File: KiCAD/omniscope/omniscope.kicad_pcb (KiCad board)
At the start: 2 copper layers, 132.8 x 90.8 mm, 40 parts, among them J1 Conn_01x08_Male, J2 Conn_01x02_Male, J3 Conn_01x02_Male, J4 Conn_01x08_Male, J5 Conn_01x08_Male, J6 Conn_01x08_Male, J7 Conn_01x08_Male, J8 Conn_01x08_Male

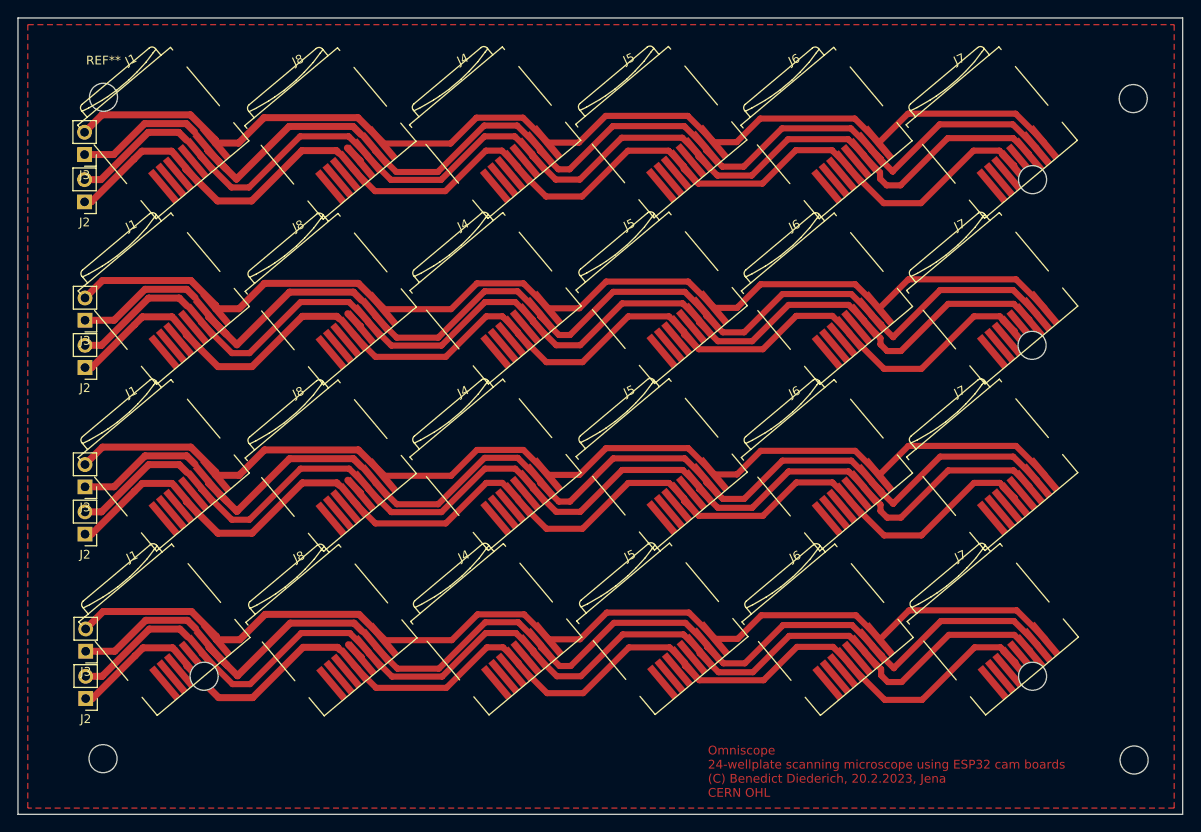
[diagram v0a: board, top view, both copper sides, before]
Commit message: Adding PCB for SD Card
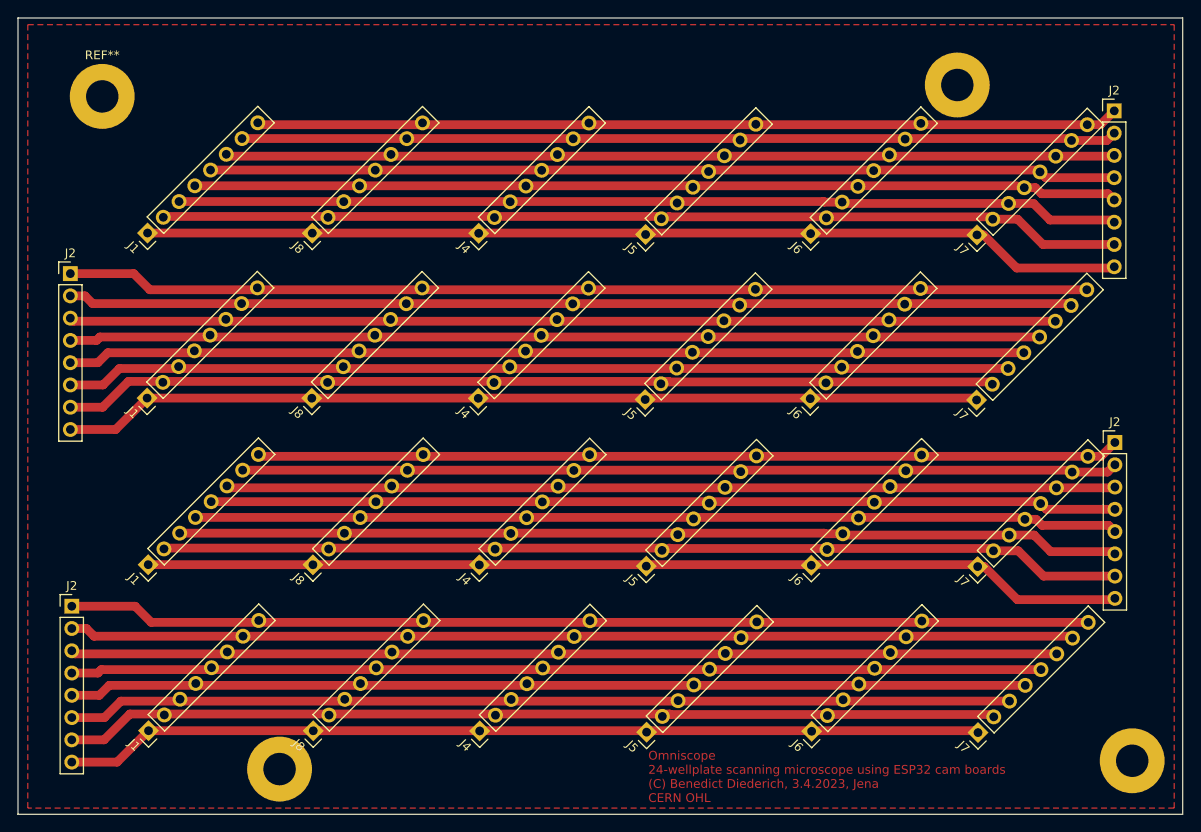
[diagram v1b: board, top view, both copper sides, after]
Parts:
- removed the ? at (126.0, 47.2)
- removed the ? at (137.5, 19.1)
- removed the ? at (137.6, 94.5)
- removed the ? at (20.0, 94.3)
- removed the ? at (31.5, 84.9)
- removed the ? at (126.0, 84.9)
- removed the ? at (126.0, 28.3)
- removed the J1 at (27.0, 21.8)
- removed the J1 at (27.1, 40.7)
- removed the J1 at (27.1, 59.7)
- removed the J2 at (18.0, 68.7)
- removed the J2 at (18.0, 49.7)
- removed the J2 at (17.9, 30.8)
- removed J3 (x4): Conn_01x02_Male, Connector_PinHeader_2.54mm:PinHeader_1x02_P2.54mm_Vertical
- removed the J4 at (64.9, 40.6)
- removed the J4 at (64.9, 59.6)
- removed the J4 at (64.8, 21.7)
- removed the J5 at (83.8, 59.6)
- removed the J5 at (83.8, 40.6)
- removed the J5 at (83.8, 21.7)
- removed the J6 at (102.7, 59.7)
- removed the J6 at (102.6, 21.8)
- removed the J6 at (102.7, 40.7)
- removed the J7 at (121.5, 21.7)
- removed the J7 at (121.5, 40.6)
- removed the J7 at (121.5, 59.6)
- removed the J8 at (46.1, 59.7)
- removed the J8 at (46.1, 40.7)
- removed the J8 at (46.1, 21.8)
- removed the REF** at (20.1, 18.9)
- added ?: , , F.Cu at (117.5, 17.5)
- added ?: , , F.Cu at (137.4, 94.6)
- added ?: , , F.Cu at (40.1, 95.5)
- added J1: Conn_01x08_Male, Connector_PinHeader_2.54mm:PinHeader_1x08_P2.54mm_Vertical, F.Cu at (25.2, 72.2)
- added J1: Conn_01x08_Male, Connector_PinHeader_2.54mm:PinHeader_1x08_P2.54mm_Vertical, F.Cu at (25.0, 53.2)
- added J1: Conn_01x08_Male, Connector_PinHeader_2.54mm:PinHeader_1x08_P2.54mm_Vertical, F.Cu at (25.1, 34.4)
- added J2: Conn_01x08_Male, Connector_PinHeader_2.54mm:PinHeader_1x08_P2.54mm_Vertical, F.Cu at (16.3, 39.0)
- added J2: Conn_01x08_Male, Connector_PinHeader_2.54mm:PinHeader_1x08_P2.54mm_Vertical, F.Cu at (135.4, 58.3)
- added J2: Conn_01x08_Male, Connector_PinHeader_2.54mm:PinHeader_1x08_P2.54mm_Vertical, F.Cu at (135.3, 20.4)
- added J4: Conn_01x08_Male, Connector_PinHeader_2.54mm:PinHeader_1x08_P2.54mm_Vertical, F.Cu at (62.9, 72.2)
- added J4: Conn_01x08_Male, Connector_PinHeader_2.54mm:PinHeader_1x08_P2.54mm_Vertical, F.Cu at (62.9, 34.4)
- added J4: Conn_01x08_Male, Connector_PinHeader_2.54mm:PinHeader_1x08_P2.54mm_Vertical, F.Cu at (62.8, 53.2)
- added J5: Conn_01x08_Male, Connector_PinHeader_2.54mm:PinHeader_1x08_P2.54mm_Vertical, F.Cu at (82.0, 72.4)
- added J5: Conn_01x08_Male, Connector_PinHeader_2.54mm:PinHeader_1x08_P2.54mm_Vertical, F.Cu at (81.9, 34.6)
- added J5: Conn_01x08_Male, Connector_PinHeader_2.54mm:PinHeader_1x08_P2.54mm_Vertical, F.Cu at (81.8, 53.4)
- added J6: Conn_01x08_Male, Connector_PinHeader_2.54mm:PinHeader_1x08_P2.54mm_Vertical, F.Cu at (100.7, 53.3)
- added J6: Conn_01x08_Male, Connector_PinHeader_2.54mm:PinHeader_1x08_P2.54mm_Vertical, F.Cu at (100.8, 72.3)
- added J6: Conn_01x08_Male, Connector_PinHeader_2.54mm:PinHeader_1x08_P2.54mm_Vertical, F.Cu at (100.7, 34.5)
- added J7: Conn_01x08_Male, Connector_PinHeader_2.54mm:PinHeader_1x08_P2.54mm_Vertical, F.Cu at (119.7, 34.6)
- added J7: Conn_01x08_Male, Connector_PinHeader_2.54mm:PinHeader_1x08_P2.54mm_Vertical, F.Cu at (119.8, 72.4)
- added J7: Conn_01x08_Male, Connector_PinHeader_2.54mm:PinHeader_1x08_P2.54mm_Vertical, F.Cu at (119.6, 53.4)
- added J8: Conn_01x08_Male, Connector_PinHeader_2.54mm:PinHeader_1x08_P2.54mm_Vertical, F.Cu at (43.9, 34.4)
- added J8: Conn_01x08_Male, Connector_PinHeader_2.54mm:PinHeader_1x08_P2.54mm_Vertical, F.Cu at (43.8, 53.2)
- added J8: Conn_01x08_Male, Connector_PinHeader_2.54mm:PinHeader_1x08_P2.54mm_Vertical, F.Cu at (44.0, 72.2)
- added REF**: MountingHole_3.7mm_Pad, MountingHole:MountingHole_3.7mm_Pad, F.Cu at (19.9, 18.8)
- J1, J4, J5, J6, J7, J8: footprint footprints:microSD_pinspacing -> Connector_PinHeader_2.54mm:PinHeader_1x08_P2.54mm_Vertical
- J2: value Conn_01x02_Male -> Conn_01x08_Male; footprint Connector_PinHeader_2.54mm:PinHeader_1x02_P2.54mm_Vertical -> Connector_PinHeader_2.54mm:PinHeader_1x08_P2.54mm_Vertical
- moved J5 13.1 mm to (82.0, 91.3), turned to 135 degrees
- moved J7 13.1 mm to (119.8, 91.4), turned to 135 degrees
- moved J4 12.9 mm to (63.0, 91.2), turned to 135 degrees
- moved J6 12.9 mm to (100.8, 91.2), turned to 135 degrees
- moved J8 12.9 mm to (44.0, 91.2), turned to 135 degrees
- moved J1 12.9 mm to (25.2, 91.1), turned to 135 degrees
- moved J2 10.7 mm to (16.4, 77.0), turned to 0 degrees
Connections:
- J1 pad 1: unconnected-(J1-Pad1) -> Net-(J1-Pin_1)
- J1 pad 2: unconnected-(J1-Pad2) -> Net-(J1-Pin_2)
- J1 pad 3: unconnected-(J1-Pad3) -> Net-(J1-Pin_3)
- J1 pad 5: unconnected-(J1-Pad5) -> Net-(J1-Pin_5)
- J2 pad 1: +3V3 -> +1V1
- J2 pad 2: GND -> +1V0
- J4 pad 1: unconnected-(J4-Pad1) -> Net-(J1-Pin_1)
- J4 pad 2: unconnected-(J4-Pad2) -> Net-(J1-Pin_2)
- J4 pad 3: unconnected-(J4-Pad3) -> Net-(J1-Pin_3)
- J4 pad 5: unconnected-(J4-Pad5) -> Net-(J1-Pin_5)
- J5 pad 1: unconnected-(J5-Pad1) -> Net-(J1-Pin_1)
- J5 pad 2: unconnected-(J5-Pad2) -> Net-(J1-Pin_2)
- J5 pad 3: unconnected-(J5-Pad3) -> Net-(J1-Pin_3)
- J5 pad 5: unconnected-(J5-Pad5) -> Net-(J1-Pin_5)
- J6 pad 1: unconnected-(J6-Pad1) -> Net-(J1-Pin_1)
- J6 pad 2: unconnected-(J6-Pad2) -> Net-(J1-Pin_2)
- J6 pad 3: unconnected-(J6-Pad3) -> Net-(J1-Pin_3)
- J6 pad 5: unconnected-(J6-Pad5) -> Net-(J1-Pin_5)
- J7 pad 1: unconnected-(J7-Pad1) -> Net-(J1-Pin_1)
- J7 pad 2: unconnected-(J7-Pad2) -> Net-(J1-Pin_2)
- J7 pad 3: unconnected-(J7-Pad3) -> Net-(J1-Pin_3)
- J7 pad 5: unconnected-(J7-Pad5) -> Net-(J1-Pin_5)
- J8 pad 1: unconnected-(J8-Pad1) -> Net-(J1-Pin_1)
- J8 pad 2: unconnected-(J8-Pad2) -> Net-(J1-Pin_2)
- J8 pad 3: unconnected-(J8-Pad3) -> Net-(J1-Pin_3)
- J8 pad 5: unconnected-(J8-Pad5) -> Net-(J1-Pin_5)
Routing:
- net Net-(J1-Pin_1): track 0.00 -> 433.6 mm
- net Net-(J1-Pin_3): track 0.00 -> 431.3 mm
- net Net-(J1-Pin_2): track 0.00 -> 431.2 mm
- net Net-(J1-Pin_5): track 0.00 -> 428.3 mm
- net +1V0: track 532.7 -> 429.6 mm
- net GND: track 522.1 -> 427.8 mm
- net +3V3: track 515.7 -> 428.2 mm
- net +1V1: track 497.2 -> 430.3 mm
- net unconnected-(J8-Pad5): track 8.89 -> 0.00 mm
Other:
- board text added: "02"
- board text added: "12"
- board text added: "13"
- board text added: "14"
- board text added: "15"
- board text added: "3V3"
- board text added: "4"
- board text added: "GND"
- board text added: "Omniscope 24-wellplate scanning microscope using ESP32 cam boards (C) Benedict Diederich, 3.4.2023, Jena CERN OHL"
- board text removed: "Omniscope 24-wellplate scanning microscope using ESP32 cam boards (C) Benedict Diederich, 20.2.2023, Jena CERN OHL"

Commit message: Adding latest CAD Drawings
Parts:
- removed ? (x3): , 
- removed the J1 at (25.2, 72.2)
- removed the J1 at (25.0, 53.2)
- removed the J1 at (25.1, 34.4)
- removed the J2 at (16.3, 39.0)
- removed the J2 at (135.4, 58.3)
- removed the J2 at (135.3, 20.4)
- removed the J4 at (62.9, 72.2)
- removed the J4 at (62.9, 34.4)
- removed the J4 at (62.8, 53.2)
- removed the J5 at (82.0, 72.4)
- removed the J5 at (81.9, 34.6)
- removed the J5 at (81.8, 53.4)
- removed the J6 at (100.7, 53.3)
- removed the J6 at (100.8, 72.3)
- removed the J6 at (100.7, 34.5)
- removed the J7 at (119.7, 34.6)
- removed the J7 at (119.8, 72.4)
- removed the J7 at (119.6, 53.4)
- removed the J8 at (43.9, 34.4)
- removed the J8 at (43.8, 53.2)
- removed the J8 at (44.0, 72.2)
- removed REF**: MountingHole_3.7mm_Pad, MountingHole:MountingHole_3.7mm_Pad
- added J1: Conn_01x08_Male, Connector_USB:USB_3.1_Brick_nogging_24_Male_Type-C_SMD_C399939, F.Cu at (128.3, 62.7)
- added J1: Conn_01x08_Male, Connector_USB:USB_3.1_Brick_nogging_24_Male_Type-C_SMD_C399939, F.Cu at (128.2, 25.0)
- added J1: Conn_01x08_Male, Connector_USB:USB_3.1_Brick_nogging_24_Male_Type-C_SMD_C399939, F.Cu at (29.0, 50.9)
- added J2: Conn_01x08_Male, Connector_PinHeader_2.54mm:PinHeader_1x08_P2.54mm_Vertical, F.Cu at (141.0, 74.4)
- added J2: Conn_01x08_Male, Connector_PinHeader_2.54mm:PinHeader_1x08_P2.54mm_Vertical, F.Cu at (140.9, 36.6)
- added J2: Conn_01x08_Male, Connector_PinHeader_2.54mm:PinHeader_1x08_P2.54mm_Vertical, F.Cu at (16.3, 39.3)
- added J4: Conn_01x08_Male, Connector_USB:USB_3.1_Brick_nogging_24_Male_Type-C_SMD_C399939, F.Cu at (90.8, 62.8)
- added J4: Conn_01x08_Male, Connector_USB:USB_3.1_Brick_nogging_24_Male_Type-C_SMD_C399939, F.Cu at (66.5, 50.9)
- added J4: Conn_01x08_Male, Connector_USB:USB_3.1_Brick_nogging_24_Male_Type-C_SMD_C399939, F.Cu at (90.7, 25.0)
- added J5: Conn_01x08_Male, Connector_USB:USB_3.1_Brick_nogging_24_Male_Type-C_SMD_C399939, F.Cu at (71.8, 25.0)
- added J5: Conn_01x08_Male, Connector_USB:USB_3.1_Brick_nogging_24_Male_Type-C_SMD_C399939, F.Cu at (85.4, 50.9)
- added J5: Conn_01x08_Male, Connector_USB:USB_3.1_Brick_nogging_24_Male_Type-C_SMD_C399939, F.Cu at (71.9, 62.8)
- added J6: Conn_01x08_Male, Connector_USB:USB_3.1_Brick_nogging_24_Male_Type-C_SMD_C399939, F.Cu at (104.2, 51.0)
- added J6: Conn_01x08_Male, Connector_USB:USB_3.1_Brick_nogging_24_Male_Type-C_SMD_C399939, F.Cu at (53.1, 62.7)
- added J6: Conn_01x08_Male, Connector_USB:USB_3.1_Brick_nogging_24_Male_Type-C_SMD_C399939, F.Cu at (53.0, 24.9)
- added J7: Conn_01x08_Male, Connector_USB:USB_3.1_Brick_nogging_24_Male_Type-C_SMD_C399939, F.Cu at (33.9, 24.9)
- added J7: Conn_01x08_Male, Connector_USB:USB_3.1_Brick_nogging_24_Male_Type-C_SMD_C399939, F.Cu at (34.0, 62.7)
- added J7: Conn_01x08_Male, Connector_USB:USB_3.1_Brick_nogging_24_Male_Type-C_SMD_C399939, F.Cu at (123.3, 51.0)
- added J8: Conn_01x08_Male, Connector_USB:USB_3.1_Brick_nogging_24_Male_Type-C_SMD_C399939, F.Cu at (47.7, 51.0)
- added J8: Conn_01x08_Male, Connector_USB:USB_3.1_Brick_nogging_24_Male_Type-C_SMD_C399939, F.Cu at (109.5, 24.9)
- added J8: Conn_01x08_Male, Connector_USB:USB_3.1_Brick_nogging_24_Male_Type-C_SMD_C399939, F.Cu at (109.6, 62.7)
- J1, J4, J5, J6, J7, J8: footprint Connector_PinHeader_2.54mm:PinHeader_1x08_P2.54mm_Vertical -> Connector_USB:USB_3.1_Brick_nogging_24_Male_Type-C_SMD_C399939
- moved J1 4.65 mm to (29.1, 88.6), turned to 90 degrees
- moved J8 4.62 mm to (47.9, 88.6), turned to 90 degrees
- moved J4 4.52 mm to (66.7, 88.6), turned to 90 degrees
- moved J7 4.49 mm to (123.4, 88.7), turned to 90 degrees
- moved J5 4.48 mm to (85.5, 88.6), turned to 90 degrees
- moved J6 4.36 mm to (104.4, 88.7), turned to 90 degrees
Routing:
- net +1V1: track 430.3 -> 457.7 mm
- net Net-(J1-Pin_1): track 433.6 -> 454.8 mm
- net Net-(J1-Pin_2): track 431.2 -> 452.0 mm
- net GND: track 427.8 -> 448.1 mm
- net +1V0: track 429.6 -> 449.0 mm
- net +3V3: track 428.2 -> 445.9 mm
- net Net-(J1-Pin_3): track 431.3 -> 448.8 mm
- net Net-(J1-Pin_5): track 428.3 -> 443.4 mm
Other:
- board text added: "Omniscope 24-wellplate scanning microscope using XIAO ESP32S3 cam boards (C) Benedict Diederich, 27.4.2023, Jena CERN OHL"
- board text removed: "Omniscope 24-wellplate scanning microscope using ESP32 cam boards (C) Benedict Diederich, 3.4.2023, Jena CERN OHL"
